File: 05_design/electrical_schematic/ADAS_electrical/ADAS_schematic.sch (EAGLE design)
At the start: 2 parts, among them U1 ARDUINO-MEGAFULL, U2 ADAFRUIT_BNO055

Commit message: Updated schematic
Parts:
- added BAT1: 24v, special:BATTERY
- added C1, C2: 1u, rcl:CPOL-EU139CLL-3R
- added R1: 27k, rcl:R-EU_0617/22
- added R2: 4k7, rcl:R-EU_0617/22
- added SW1: CT10-XXXX-A2, switch-coto:CT10-XXXX-A2
- added U$2: LOGIC_LEVEL_CONVERTER, SparkFun-Boards:LOGIC_LEVEL_CONVERTER
- added U3: SICK_PLS, BNO055_breakout:SICK_PLS
- added U4: ESP12E_DEVKIT, ESP12E_DEVKIT:ESP12E_DEVKIT
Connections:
- new net +24V: R1.2, SW1.1
- new net +3V3: C2.+, U$2.LV, U1.3.3V, U4.3V3@0
- new net ESP_RX: U$2.LV_RXO_1, U4.RX
- new net ESP_TX: U$2.LV_TXI_1, U4.TX
- new net MTR_L: U1.9
- new net MTR_R: U1.10
- new net N$1: BAT1.+, SW1.2
- new net RX1: U1.19(RX1), U3.TX
- new net RX2: U$2.HV_TXO_1, U1.17(RX2)
- new net TX1: U1.18(TX1), U3.RX
- new net TX2: U$2.HV_RXI_1, U1.16(TX2)
- new net VBAT_5V: C1.+, R1.1, R2.2, U1.A2
- net +5V: now also U$2.HV, U3.VCC
- net GND: now also BAT1.-, C1.-, C2.-, R2.1, U$2.GND, U$2.GND@2, U3.GND, U4.GND@1
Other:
- note added: "3.3V <> 5V Level Shifter"
- note added: "Battery"
- note added: "Battery Monitor"
- note added: "Battery VBAT_5V 33.7V 5V 28V 4.15V 24V 3.56V 12V 1.78V 0V 0V"
- note added: "IMU"
- note added: "Laser Scanner"
- note added: "MPU"
- note added: "Optional:"
- note added: "WiFi Module"

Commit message: Added h-bridges, encoder and buck-converter
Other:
- note added: "5V DC/DC-Converter"
- note added: "Christoph Jurczyk"
- note added: "Encoder left"
- note added: "Encoder right"
- note added: "H-Bridge left"
- note added: "H-Bridge right"
- note added: "I suggest a buck-converter"
- note added: "Waiting for schematics from A.Menslage"
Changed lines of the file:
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@@
 <wire x1="177.8" y1="83.82" x2="7.62" y2="83.82" width="0.1524" layer="94" style="shortdash"/>
 <text x="93.98" y="73.66" size="3.81" layer="91" align="bottom-center">Optional:</text>
+<text x="246.38" y="241.3" size="3.81" layer="91" align="bottom-center">H-Bridge right</text>
+<text x="185.42" y="241.3" size="3.81" layer="91" align="bottom-center">H-Bridge left</text>
+<text x="185.42" y="190.5" size="3.81" layer="91" align="bottom-center">Encoder left</text>
+<text x="243.84" y="190.5" size="3.81" layer="91" align="bottom-center">Encoder right</text>
+<text x="238.76" y="119.38" size="3.81" layer="91" align="bottom-center">5V DC/DC-Converter</text>
+<text x="218.44" y="111.76" size="1.778" layer="91" align="top-left">I suggest a buck-converter</text>
+<text x="344.424" y="20.32" size="2.1844" layer="94">Christoph Jurczyk</text>
+<text x="203.2" y="177.8" size="1.778" layer="91" align="top-left">Waiting for schematics from A.Menslage</text>
+<text x="200.66" y="231.14" size="1.778" layer="91" align="top-left">Waiting for schematics from A.Menslage</text>
 </plain>
 <instances>

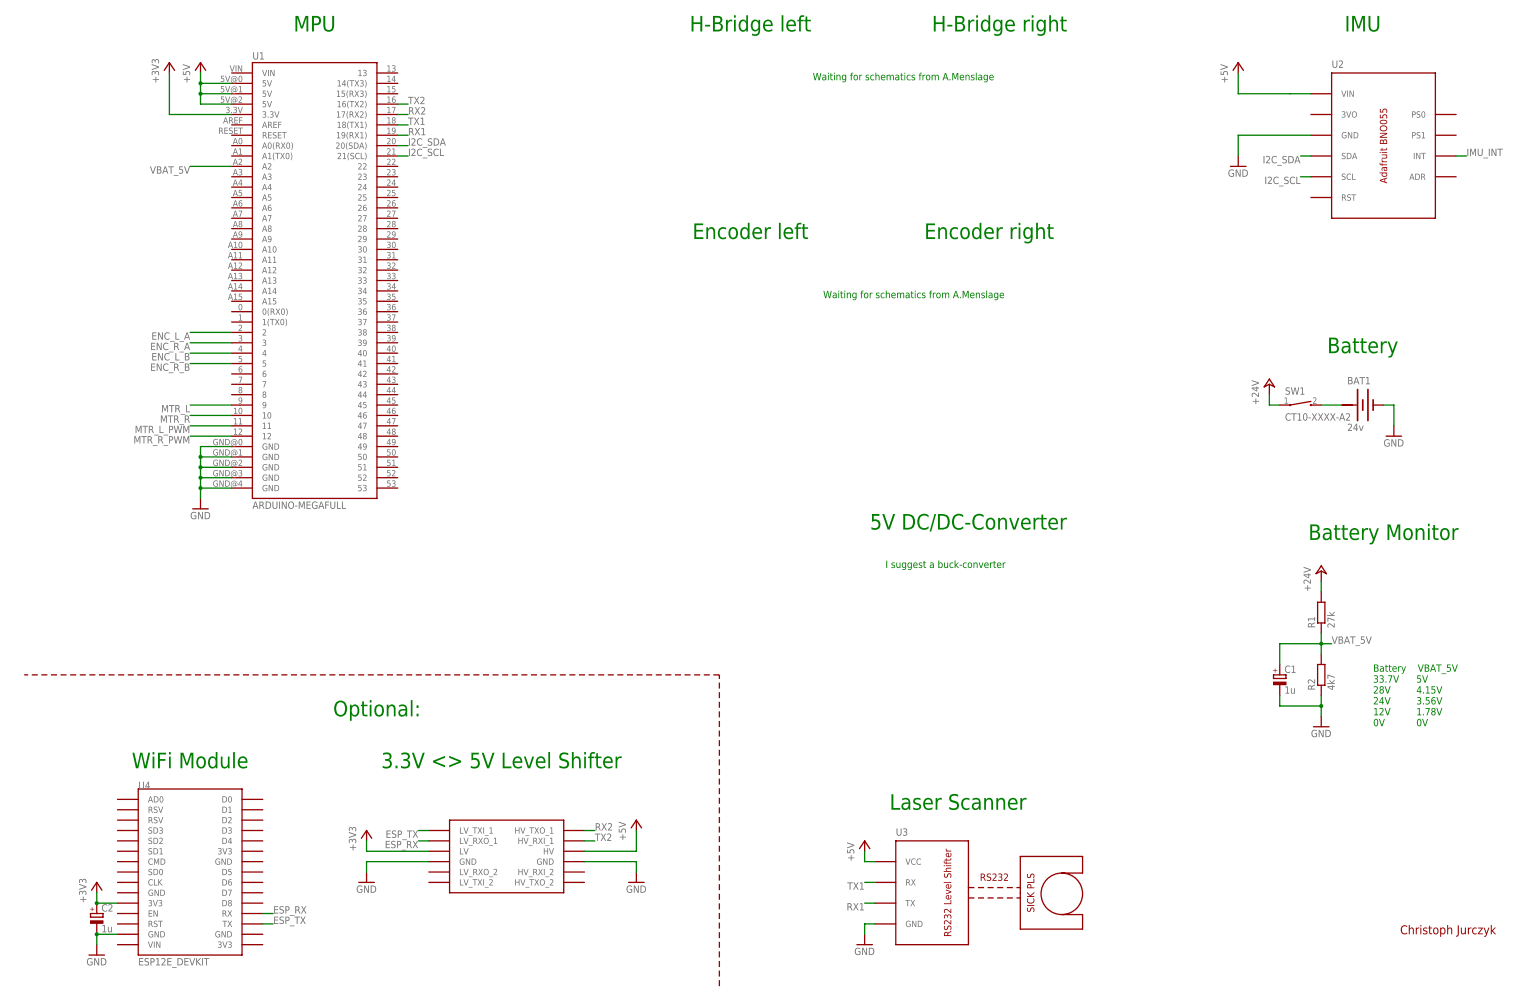
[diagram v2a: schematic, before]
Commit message: Added H-Bridge and Encoders
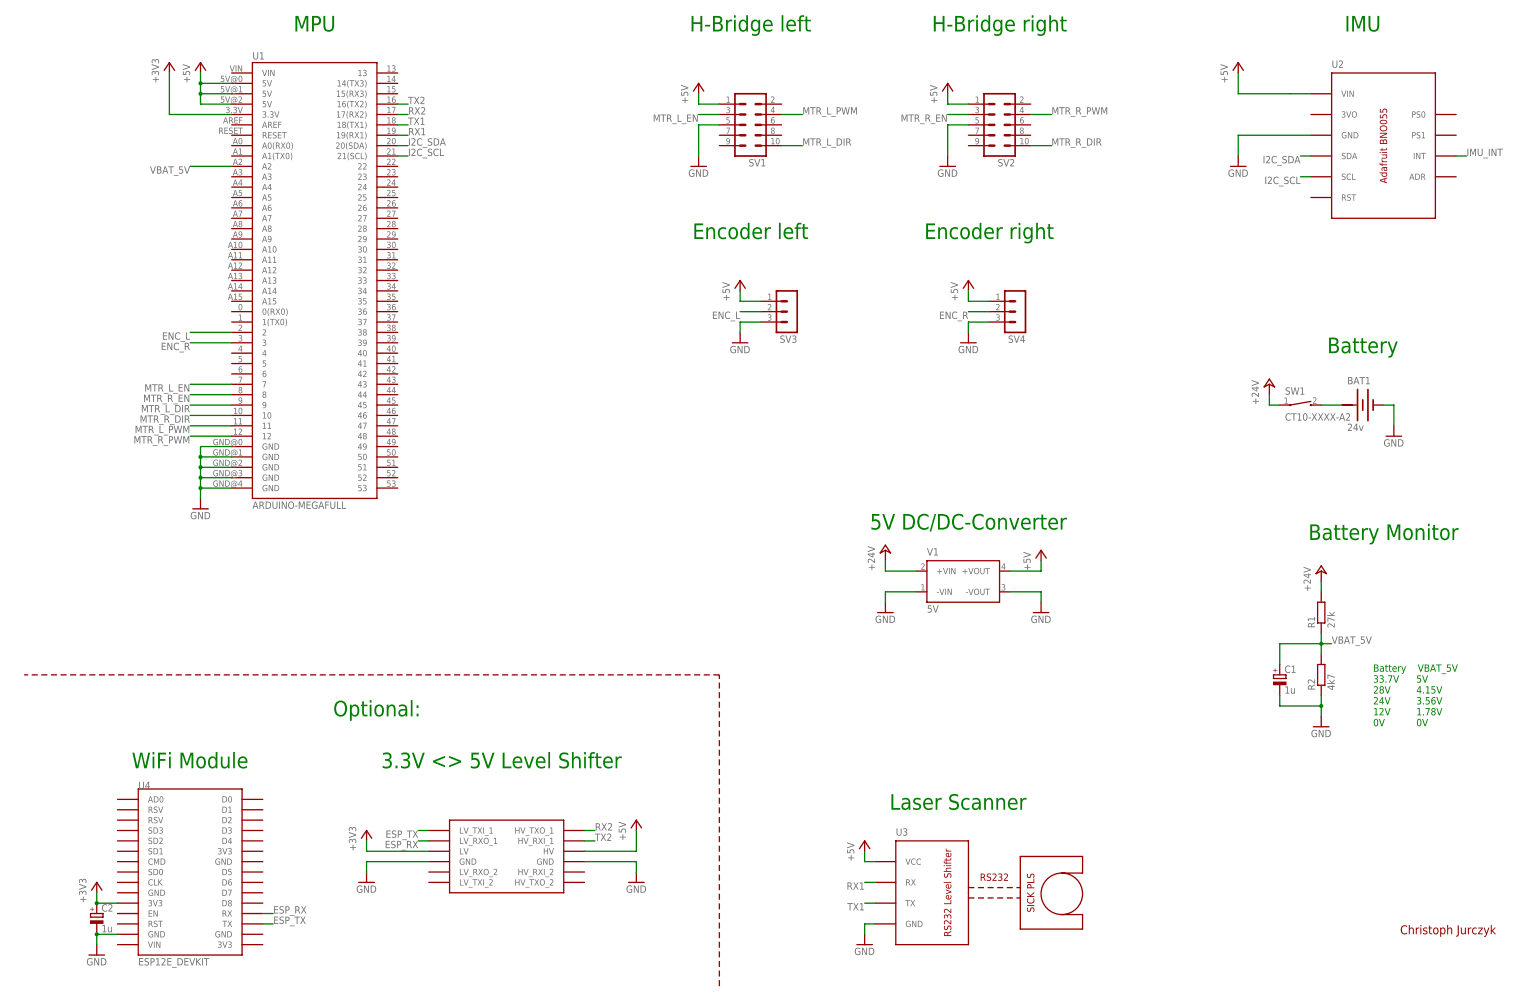
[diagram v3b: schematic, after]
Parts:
- added SV1, SV2: (no value), con-ml:ML10
- added SV3, SV4: (no value), con-lstb:MA03-1
- added V1: 5V, traco-electronic:TME0505S
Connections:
- removed net ENC_L_A: U1.2
- removed net ENC_L_B: U1.4
- removed net ENC_R_A: U1.3
- removed net ENC_R_B: U1.5
- removed net MTR_L: U1.9
- removed net MTR_R: U1.10
- new net ENC_L: SV3.2, U1.2
- new net ENC_R: SV4.2, U1.3
- new net MTR_L_DIR: SV1.10, U1.9
- new net MTR_L_EN: SV1.3, U1.7
- new net MTR_R_DIR: SV2.10, U1.10
- new net MTR_R_EN: SV2.3, U1.8
- net +24V: now also V1.+VIN
- net +5V: now also SV1.1, SV2.1, SV3.1, SV4.1, V1.+VOUT
- net GND: now also SV1.5, SV2.5, SV3.3, SV4.3, V1.-VIN, V1.-VOUT
- net MTR_L_PWM: now also SV1.4
- net MTR_R_PWM: now also SV2.4
- net RX1: now also U3.RX; no longer U3.TX
- net TX1: now also U3.TX; no longer U3.RX
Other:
- note removed: "I suggest a buck-converter"
- note removed: "Waiting for schematics from A.Menslage"

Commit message: Adapted electrical schematic to two chip solution
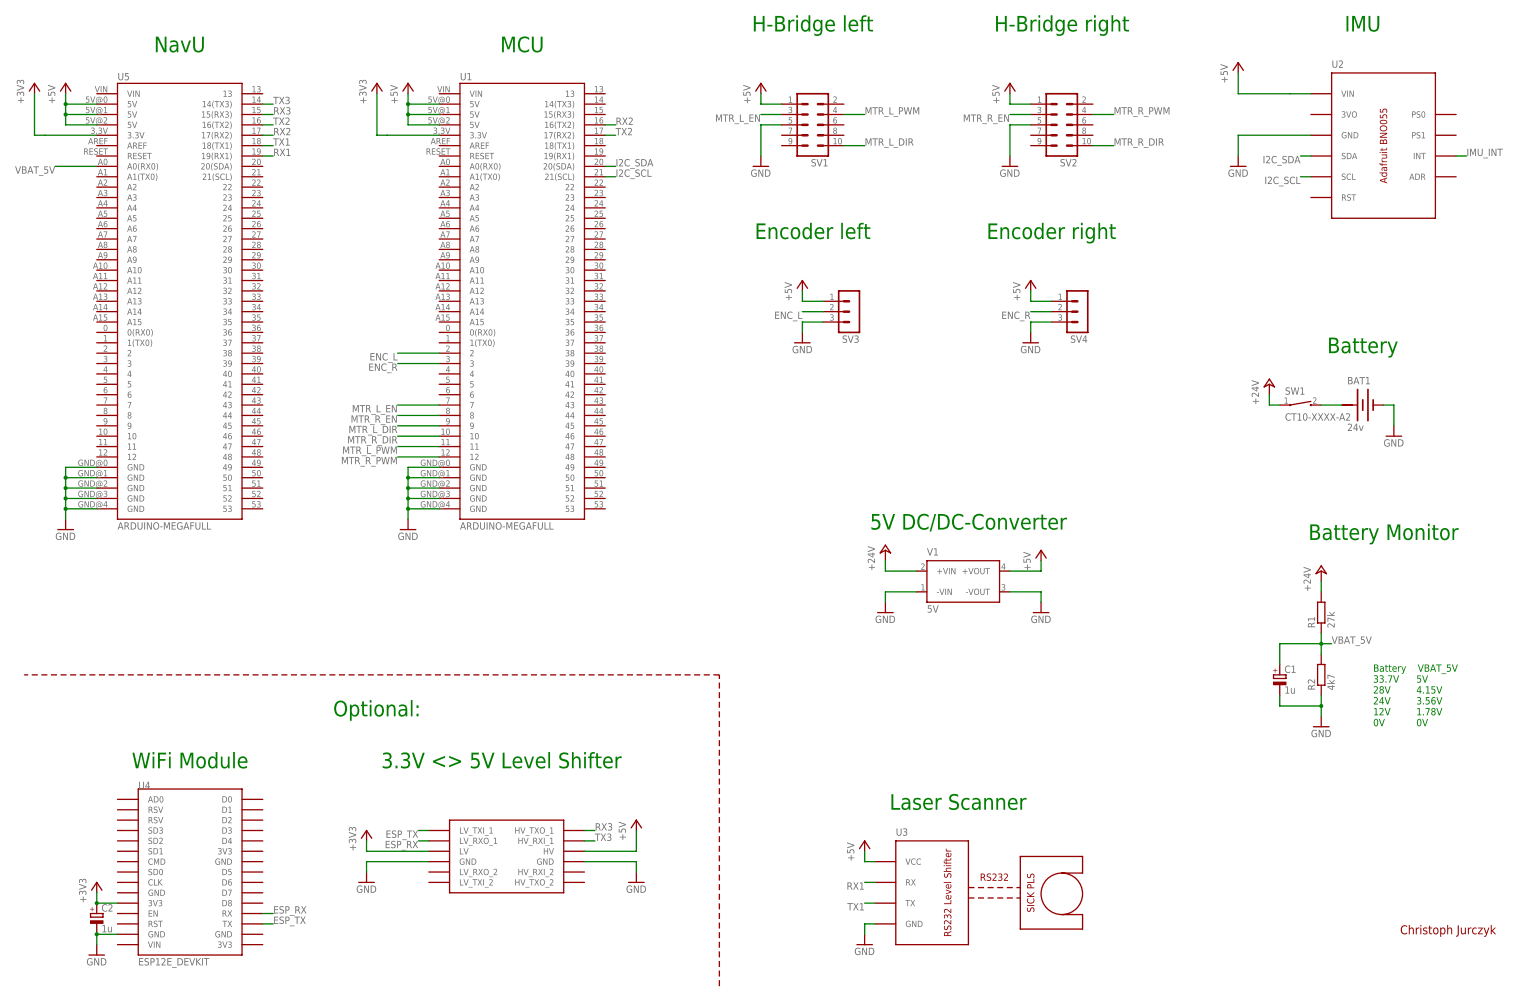
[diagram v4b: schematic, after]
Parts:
- added U5: ARDUINO-MEGAFULL, SparkFun-Boards:ARDUINO-MEGAFULL
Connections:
- new net RX3: U$2.HV_TXO_1, U5.15(RX3)
- new net TX3: U$2.HV_RXI_1, U5.14(TX3)
- net +3V3: now also U5.3.3V
- net +5V: now also U5.5V@0, U5.5V@1, U5.5V@2
- net GND: now also U5.GND@0, U5.GND@1, U5.GND@2, U5.GND@3, U5.GND@4
- net RX1: now also U5.19(RX1); no longer U1.19(RX1)
- net RX2: now also U1.16(TX2), U5.17(RX2); no longer U$2.HV_TXO_1, U1.17(RX2)
- net TX1: now also U5.18(TX1); no longer U1.18(TX1)
- net TX2: now also U1.17(RX2), U5.16(TX2); no longer U$2.HV_RXI_1, U1.16(TX2)
- net VBAT_5V: now also U5.A0(RX0); no longer U1.A2
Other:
- note added: "MCU"
- note added: "NavU"
- note removed: "MPU"
- moved on the sheet: SV1, SV2, SV3, SV4, U1
